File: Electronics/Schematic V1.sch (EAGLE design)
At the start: 2 parts, among them J1 SSW-130-01-G-S, J2 SSW-130-01-G-S

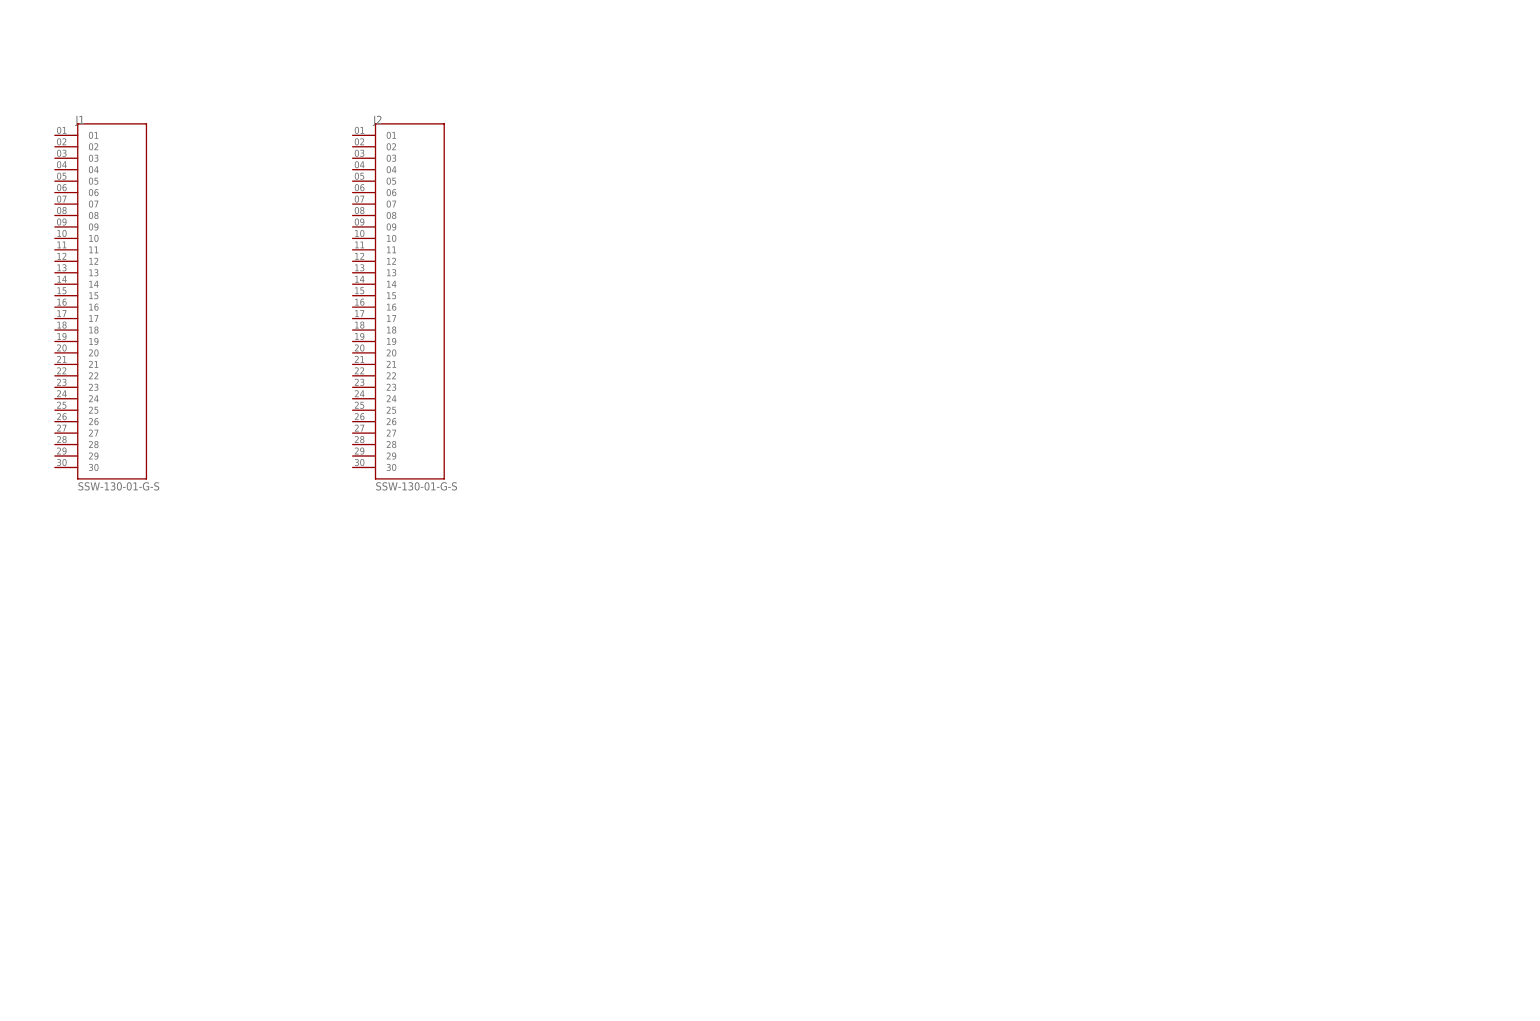
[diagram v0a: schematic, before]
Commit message: Added BOM File & Updated Schematic
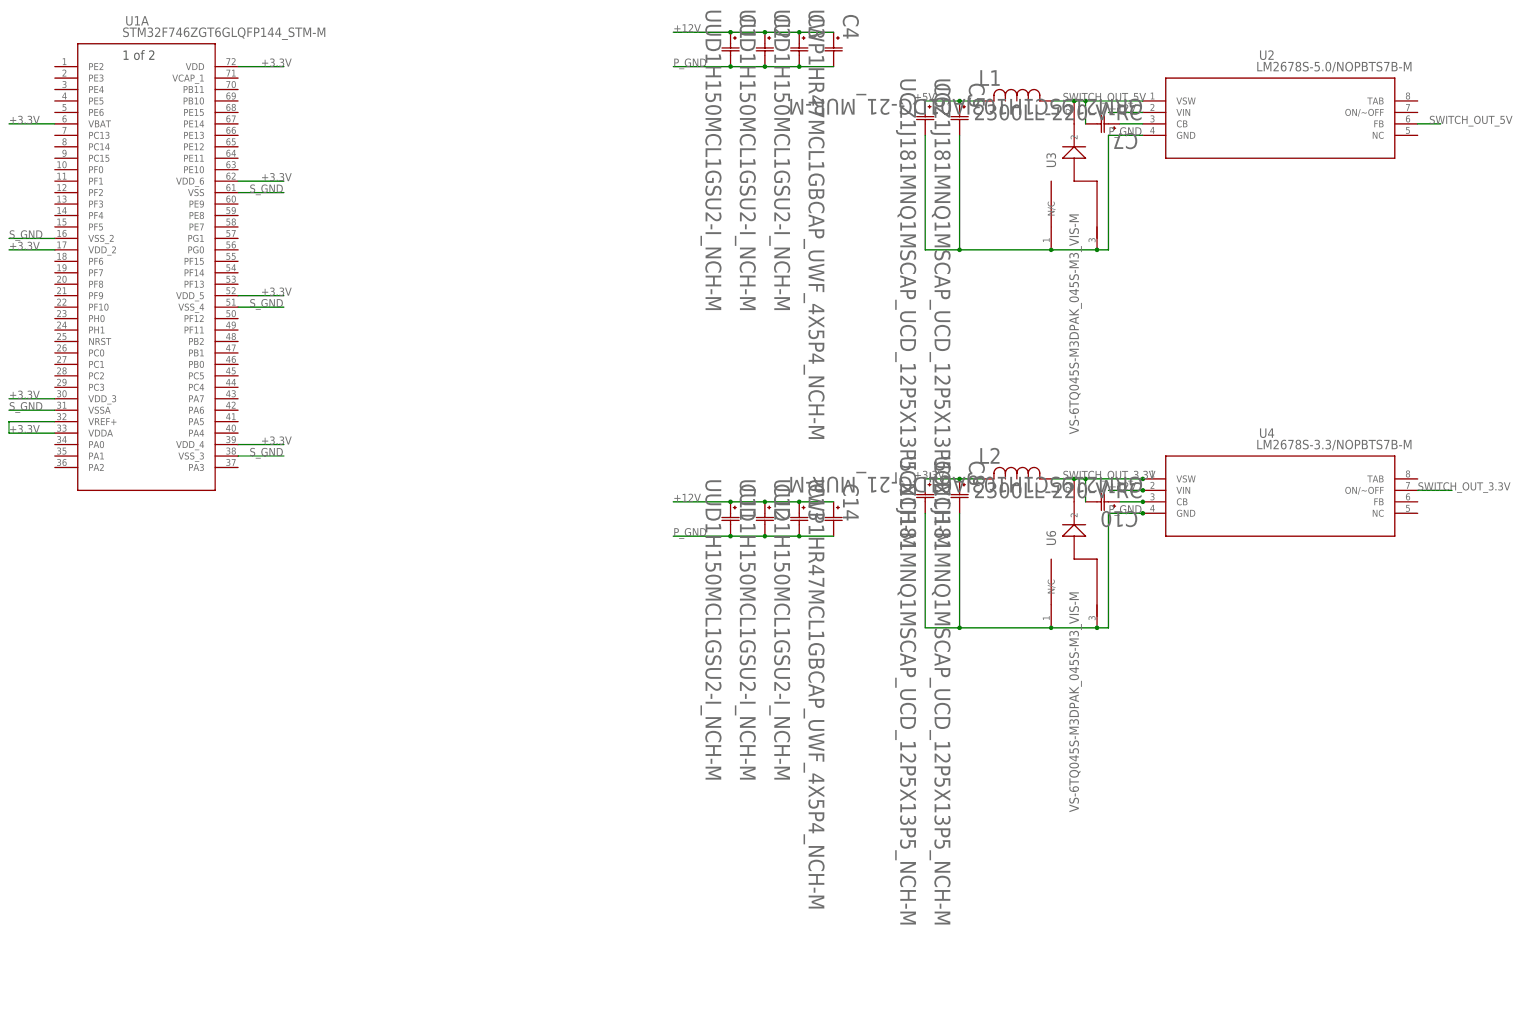
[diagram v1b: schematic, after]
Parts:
- removed J1, J2: SSW-130-01-G-S, SSW-130-01-G-S:SSW-130-01-G-S
- added C1, C11, C12, C13, C2, C3: UUD1H150MCL1GSU2-I_NCH-M, SSW-130-01-G-S:UUD1H150MCL1GSU2-I_NCH-M
- added C10, C7: GRM2195C1H103JA01DG-21_MUR-M, SSW-130-01-G-S:GRM2195C1H103JA01DG-21_MUR-M
- added C14, C4: UWP1HR47MCL1GBCAP_UWF_4X5P4_NCH-M, SSW-130-01-G-S:UWP1HR47MCL1GBCAP_UWF_4X5P4_NCH-M
- added C5, C6, C8, C9: UCZ1J181MNQ1MSCAP_UCD_12P5X13P5_NCH-M, SSW-130-01-G-S:UCZ1J181MNQ1MSCAP_UCD_12P5X13P5_NCH-M
- added L1, L2: 2300LL-220-V-RC, SSW-130-01-G-S:2300LL-220-V-RC
- added U1: STM32F746ZGT6GLQFP144_STM-M, SSW-130-01-G-S:STM32F746ZGT6GLQFP144_STM-M
- added U2: LM2678S-5.0/NOPBTS7B-M, SSW-130-01-G-S:LM2678S-5.0/NOPBTS7B-M
- added U3, U6: VS-6TQ045S-M3DPAK_045S-M3_VIS-M, SSW-130-01-G-S:VS-6TQ045S-M3DPAK_045S-M3_VIS-M
- added U4: LM2678S-3.3/NOPBTS7B-M, SSW-130-01-G-S:LM2678S-3.3/NOPBTS7B-M
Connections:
- new net +12V: C1.1, C11.1, C12.1, C13.1, C14.1, C2.1, C3.1, C4.1, U2.VIN, U4.VIN
- new net +3.3V: C8.1, C9.1, L2.2, U1A.VBAT, U1A.VDD, U1A.VDDA, U1A.VDD_2, U1A.VDD_3, U1A.VDD_4, U1A.VDD_5, U1A.VDD_6, U1A.VREF+
- new net +5V: C5.1, C6.1, L1.2
- new net N$1: C10.1, U4.CB
- new net N$2: C7.1, U2.CB
- new net P_GND: C1.2, C11.2, C12.2, C13.2, C14.2, C2.2, C3.2, C4.2, C5.2, C6.2, C8.2, C9.2, U2.GND, U3.ANODE, U3.N/C, U4.GND, U6.ANODE, U6.N/C
- new net SWITCH_OUT_3.3V: C10.2, L2.1, U4.ON/~OFF, U4.VSW, U6.2
- new net SWITCH_OUT_5V: C7.2, L1.1, U2.FB, U2.VSW, U3.2
- new net S_GND: U1A.VSS, U1A.VSSA, U1A.VSS_2, U1A.VSS_3, U1A.VSS_4

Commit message: Added A4 + Updated Schematic
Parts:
- added C15, C16, C17, C18, C19, C20, C21, C22, C23, C24, C25, C26, C27, C28, C29, C30, C32: 0.1uF, SparkFun-Capacitors:1.0UF-0805-25V-10%
- added C31, C33: 1.0uF, SparkFun-Capacitors:1.0UF-0805-25V-10%
- added C34, C35: 2.2uF, SparkFun-Capacitors:2.2UF-0805-25V-(+80/-20%)
- added C36: 4.7uF, SparkFun-Capacitors:2.2UF-0805-25V-(+80/-20%)
- added R1: 33k, SparkFun-Resistors:33KOHM-0603-1/10W-1%
- added R2: 68.1k, SparkFun-Resistors:68.1KOHM-0603-1/10W-1%
- added U5: STM32F207VGT6TR, SSW-130-01-G-S:STM32F207VGT6TR
- U1: value STM32F746ZGT6GLQFP144_STM-M -> STM32F207VGT6TR; device SSW-130-01-G-S:STM32F746ZGT6GLQFP144_STM-M -> SSW-130-01-G-S:STM32F207VGT6TR
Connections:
- new net N$4: C35.2, U5C.VCAP_1
- new net N$5: C34.2, U5C.VCAP_2
- new net S_GND1: C32.1, C33.1
- new net V_ON: R1.2, R2.1, U2.ON/~OFF, U4.ON/~OFF
- net +12V: now also R2.2
- net +3.3V: now also C15.2, C16.2, C17.2, C18.2, C19.2, C20.2, C21.2, C22.2, C23.2, C24.2, C25.2, C26.2, C27.2, C28.2, C29.2, C30.2, C31.2, C32.2, C33.2, C36.2, U5C.VBAT, U5C.VDD, U5C.VDDA, U5C.VDD_2, U5C.VDD_3, U5C.VDD_4, U5C.VDD_5, U5C.VDD_6, U5C.VREF+; no longer U1A.VBAT, U1A.VDD, U1A.VDDA, U1A.VDD_2, U1A.VDD_3, U1A.VDD_4, U1A.VDD_5, U1A.VDD_6, U1A.VREF+
- net P_GND: now also R1.1
- net SWITCH_OUT_3.3V: now also U4.FB; no longer U4.ON/~OFF
- net S_GND: now also C15.1, C16.1, C17.1, C18.1, C19.1, C20.1, C21.1, C22.1, C23.1, C24.1, C25.1, C26.1, C27.1, C28.1, C29.1, C30.1, C31.1, C34.1, C35.1, C36.1, U5C.VSS, U5C.VSSA, U5C.VSS_2, U5C.VSS_3; no longer U1A.VSS, U1A.VSSA, U1A.VSS_2, U1A.VSS_3, U1A.VSS_4
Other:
- note added: "STM32 Power Pins"
- note added: "VDD Capacitors"

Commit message: Updated Schematic with Main Features
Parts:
- added C37: 10uF, SparkFun-Capacitors:10UF-0805-10V-10%
- added C38: 0.1uF, rcl:C-USC0805
- added C39: 4.7nF, rcl:C-USC0805
- added C40: 10pF, SparkFun-Capacitors:10UF-0805-10V-10%
- added C41, C42, C43, C44: 4.7uF, rcl:C-USC0805
- added C45: (no value), rcl:C-USC0805
- added C46, C47, C48, C49, C54, C59: 1.0uF, SparkFun-Capacitors:1.0UF-0805-25V-10%
- added C50, C51, C52, C53, C55, C56, C57, C58: 0.1uF, SparkFun-Capacitors:1.0UF-0805-25V-10%
- added CR1: SL03-GS18CR_SL03_VIS-M, SSW-130-01-G-S:SL03-GS18CR_SL03_VIS-M
- added D1, D2, D3, D4, D5, D6: 250mA/100V, SparkFun-DiscreteSemi:DIODE-BAS16J
- added J1: PJ-202AH, SSW-130-01-G-S:PJ-202AH
- added L3: 7443551131IND_1365-WE-HCI_WRE-M, SSW-130-01-G-S:7443551131IND_1365-WE-HCI_WRE-M
- added R10, R12, R20, R22: 37k, rcl:R-US_R0805
- added R11, R13, R16, R19, R21, R23, R26, R9: 10k, rcl:R-US_R0805
- added R14, R15, R24, R25: 73k, rcl:R-US_R0805
- added R17, R18, R27, R28, R29, R30: 2.25k, rcl:R-US_R0805
- added R3: 10, rcl:R-US_R0805
- added R31, R32, R33, R34, R35, R36, R37, R38: 330, rcl:R-US_R0805
- added R39, R42, R45, R48, R51, R54, R57, R60: 500, rcl:R-US_R0805
- added R4: 1.5M, rcl:R-US_R0805
- added R40, R43, R46, R49, R52, R55, R58, R61: 75k, rcl:R-US_R0805
- added R41, R44, R47, R50, R53, R56, R59, R62: 25k, rcl:R-US_R0805
- added R5: 121k, rcl:R-US_R0805
- added R6: 100k, rcl:R-US_R0805
- added R7: 3352T-1-105LF, SSW-130-01-G-S:3352T-1-105LF
- added R8: 89k, rcl:R-US_R0805
- added U10, U17, U18, U19: SN65LBC175ADD16-M, SSW-130-01-G-S:SN65LBC175ADD16-M
- added U11, U8: OPA4205APWRTSSOP14_PW_R-PDSO-G14_TEX-M, SSW-130-01-G-S:OPA4205APWRTSSOP14_PW_R-PDSO-G14_TEX-M
- added U12, U7: SN75ALS174ADWRDW20-M, SSW-130-01-G-S:SN75ALS174ADWRDW20-M
- added U13, U14: SN75468DRD0016A_M, SSW-130-01-G-S:SN75468DRD0016A_M
- added U15, U16: ACSL-6400-00TESOIC_6400-00TE-M, SSW-130-01-G-S:ACSL-6400-00TESOIC_6400-00TE-M
- added U9: TPS63700DRCR, SSW-130-01-G-S:TPS63700DRCR
- L1, L2: value 2300LL-220-V-RC -> 2300HT-220-H-RC; device SSW-130-01-G-S:2300LL-220-V-RC -> SSW-130-01-G-S:2300HT-220-H-RC
- R1: value 33k -> 25k
- R2: value 68.1k -> 75k; device SparkFun-Resistors:68.1KOHM-0603-1/10W-1% -> rcl:R-US_R0805
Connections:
- removed net +12V: C1.1, C11.1, C12.1, C13.1, C14.1, C2.1, C3.1, C4.1, R2.2, U2.VIN, U4.VIN
- removed net S_GND1: C32.1, C33.1
- new net +14V: C1.1, C11.1, C12.1, C13.1, C14.1, C2.1, C3.1, C4.1, J1.1, R2.2, R39.2, R40.2, R42.2, R43.2, R45.2, R46.2, R48.2, R49.2, R51.2, R52.2, R54.2, R55.2, R57.2, R58.2, R60.2, R61.2, R8.2, U2.VIN, U4.VIN, U8.V+
- new net +24V: R17.2, R18.2, R27.2, R28.2, R29.2, R30.2, U13.COM, U14.COM
- new net -15V: C41.1, C42.1, C43.1, C44.1, CR1.2, R4.1, R6.2, U8.V-, U9.OUT
- new net 1.65V_REF: R13.1, R19.1, R23.1, R9.1, U8.-IN_1, U8.OUT_1
- new net 14V-24V_GND: J1.2, J1.3, R1.1, U13.E, U14.E
- new net ABS_ENC_OUT_GPIO_1: U10.4Y
- new net ABS_ENC_OUT_GPIO_2: U17.4Y
- new net ABS_ENC_OUT_HI_1: R33.1, U10.4A
- new net ABS_ENC_OUT_HI_2: R37.1, U17.4A
- new net ABS_ENC_OUT_LO_1: R33.2, U10.4B
- new net ABS_ENC_OUT_LO_2: R37.2, U17.4B
- new net ALARM_RST_AN_1: U13.5C
- new net ALARM_RST_AN_2: U14.5C
- new net ALARM_RST_GPIO_1: U13.5B
- new net ALARM_RST_GPIO_2: U14.5B
- new net ALO_AN_A_1: D1.A, U15.CATHODE1
- new net ALO_AN_A_2: D4.A, U16.CATHODE1
- new net ALO_AN_B_1: D2.A, U15.CATHODE2
- new net ALO_AN_B_2: D5.A, U16.CATHODE2
- new net ALO_AN_C_1: D3.A, U15.CATHODE3
- new net ALO_AN_C_2: D6.A, U16.CATHODE3
- new net ALO_GPIO_A_1: U15.V01
- new net ALO_GPIO_A_2: U16.V01
- new net ALO_GPIO_B_1: U15.V02
- new net ALO_GPIO_B_2: U16.V02
- new net ALO_GPIO_C_1: U15.V03
- new net ALO_GPIO_C_2: U16.V03
- new net CLR_EN_GPIO: U12.3/42N, U7.3/42N
- new net CLR_GPIO_1: U7.3A
- new net CLR_GPIO_2: U12.3A
- new net CLR_HI_1: U7.3Y
- new net CLR_HI_2: U12.3Y
- new net CLR_LO_1: U7.3Z
- new net CLR_LO_2: U12.3Z
- new net DIR_GPIO_1: U7.2A
- new net DIR_GPIO_2: U12.2A
- new net DIR_HI_1: U7.2Y
- new net DIR_HI_2: U12.2Y
- new net DIR_LO_1: U7.2Z
- new net DIR_LO_2: U12.2Z
- new net ENC_PUL_OUT_A_GPIO_1: U10.1Y
- new net ENC_PUL_OUT_A_GPIO_2: U17.1Y
- new net ENC_PUL_OUT_A_HI_1: R31.1, U10.1A
- new net ENC_PUL_OUT_A_HI_2: R35.1, U17.1A
- new net ENC_PUL_OUT_A_LO_1: R31.2, U10.1B
- new net ENC_PUL_OUT_A_LO_2: R35.2, U17.1B
- new net ENC_PUL_OUT_B_GPIO_1: U10.2Y
- new net ENC_PUL_OUT_B_GPIO_2: U17.2Y
- new net ENC_PUL_OUT_B_HI_1: R32.2, U10.2A
- new net ENC_PUL_OUT_B_HI_2: R36.2, U17.2A
- new net ENC_PUL_OUT_B_LO_1: R32.1, U10.2B
- new net ENC_PUL_OUT_B_LO_2: R36.1, U17.2B
- new net ENC_PUL_OUT_C_GPIO_1: U10.3Y
- new net ENC_PUL_OUT_C_GPIO_2: U17.3Y
- new net ENC_PUL_OUT_C_HI_1: R34.2, U10.3A
- new net ENC_PUL_OUT_C_HI_2: R38.2, U17.3A
- new net ENC_PUL_OUT_C_LO_1: R34.1, U10.3B
- new net ENC_PUL_OUT_C_LO_2: R38.1, U17.3B
- new net FRWD_DRIVE_EN_AN_1: U13.3C
- new net FRWD_DRIVE_EN_AN_2: U14.3C
- new net FRWD_DRIVE_EN_GPIO_1: U13.3B
- new net FRWD_DRIVE_EN_GPIO_2: U14.3B
- new net FRWD_EX_TORQUE_LIM_EN_AN_1: U13.6C
- new net FRWD_EX_TORQUE_LIM_EN_AN_2: U14.6C
- new net FRWD_EX_TORQUE_LIM_EN_GPIO_1: U13.6B
- new net FRWD_EX_TORQUE_LIM_EN_GPIO_2: U14.6B
- new net GEN_PURPOSE_OUT_GPIO_A_1: U18.1Y
- new net GEN_PURPOSE_OUT_GPIO_A_2: U19.1Y
- new net GEN_PURPOSE_OUT_GPIO_B_1: U18.2Y
- new net GEN_PURPOSE_OUT_GPIO_B_2: U19.2Y
- new net GEN_PURPOSE_OUT_GPIO_C_1: U18.3Y
- new net GEN_PURPOSE_OUT_GPIO_C_2: U19.3Y
- new net GEN_PURPOSE_OUT_HI_A_1: R39.1, U18.1A
- new net GEN_PURPOSE_OUT_HI_A_2: R51.1, U19.1A
- new net GEN_PURPOSE_OUT_HI_B_1: R42.1, U18.2A
- new net GEN_PURPOSE_OUT_HI_B_2: R54.1, U19.2A
- new net GEN_PURPOSE_OUT_HI_C_1: R45.1, U18.3A
- new net GEN_PURPOSE_OUT_HI_C_2: R57.1, U19.3A
- new net GEN_PURPOSE_OUT_LO_A_1: C50.2, R40.1, R41.2, U18.1B
- new net GEN_PURPOSE_OUT_LO_A_2: C55.2, R52.1, R53.2, U19.1B
- new net GEN_PURPOSE_OUT_LO_B_1: C51.2, R43.1, R44.2, U18.2B
- new net GEN_PURPOSE_OUT_LO_B_2: C56.2, R55.1, R56.2, U19.2B
- new net GEN_PURPOSE_OUT_LO_C_1: C52.2, R46.1, R47.2, U18.3B
- new net GEN_PURPOSE_OUT_LO_C_2: C57.2, R58.1, R59.2, U19.3B
- new net N$10: C40.2, R4.2, R5.1, U9.FB
- new net N$11: C40.1, R6.1
- new net N$12: R7.2, U8.+IN_1
- new net N$13: R7.3, R8.1
- new net N$15: R11.2, R12.2, U8.+IN_2
- new net N$17: R13.2, R14.2, U8.-IN_4
- new net N$18: R15.2, R16.2, U8.+IN_4
- new net N$20: D1.C, R17.1, U15.ANODE1
- new net N$21: R19.2, R20.2, U11.-IN_2
- new net N$22: R21.2, R22.2, U11.+IN_2
- new net N$23: R23.2, R24.2, U11.-IN_4
- new net N$24: R25.2, R26.2, U11.+IN_4
- new net N$25: D2.C, R18.1, U15.ANODE2
- new net N$26: D3.C, R27.1, U15.ANODE3
- new net N$27: D4.C, R28.1, U16.ANODE1
- new net N$28: D5.C, R29.1, U16.ANODE2
- new net N$29: D6.C, R30.1, U16.ANODE3
- new net N$3: C39.1, U9.COMP
- new net N$6: C38.1, R3.1, U9.EN, U9.VIN
- new net N$7: CR1.1, L3.2, U9.SW
- new net N$8: R10.2, R9.2, U8.-IN_2
- new net N$9: C45.1, R5.2, U9.VREF
- new net POS_EN_GPIO: U12.1/2EN, U7.1/2EN
- new net PROP_CONTROL_EN_AN_1: U13.2C
- new net PROP_CONTROL_EN_AN_2: U14.2C
- new net PROP_CONTROL_EN_GPIO_1: U13.2B
- new net PROP_CONTROL_EN_GPIO_2: U14.2B
- new net PULSE_GPIO_1: U7.1A
- new net PULSE_GPIO_2: U12.1A
- new net PULSE_HI_1: U7.1Y
- new net PULSE_HI_2: U12.1Y
- new net PULSE_LO_1: U7.1Z
- new net PULSE_LO_2: U12.1Z
- new net REVERSE_DRIVE_EN_AN_1: U13.4C
- new net REVERSE_DRIVE_EN_AN_2: U14.4C
- new net REVERSE_DRIVE_EN_GPIO_1: U13.4B
- new net REVERSE_DRIVE_EN_GPIO_2: U14.4B
- new net REVERSE_EX_TORQUE_LIM_EN_AN_1: U13.7C
- new net REVERSE_EX_TORQUE_LIM_EN_AN_2: U14.7C
- new net REVERSE_EX_TORQUE_LIM_EN_GPIO_1: U13.7B
- new net REVERSE_EX_TORQUE_LIM_EN_GPIO_2: U14.7B
- new net SERVO_ALARM_OUT_GPIO_1: U18.4Y
- new net SERVO_ALARM_OUT_GPIO_2: U19.4Y
- new net SERVO_ALARM_OUT_HI_1: R48.1, U18.4A
- new net SERVO_ALARM_OUT_HI_2: R60.1, U19.4A
- new net SERVO_ALARM_OUT_LO_1: C53.2, R49.1, R50.2, U18.4B
- new net SERVO_ALARM_OUT_LO_2: C58.2, R61.1, R62.2, U19.4B
- new net SERVO_EN_AN_1: U13.1C
- new net SERVO_EN_AN_2: U14.1C
- new net SERVO_EN_GPIO_1: U13.1B
- new net SERVO_EN_GPIO_2: U14.1B
- new net SPEED_ANALOG_1: R12.1, U8.OUT_2
- new net SPEED_ANALOG_2: R22.1, U11.OUT_2
- new net SPEED_DAC_1: R11.1
- new net SPEED_DAC_2: R21.1
- new net TORQUE_ANALOG_1: R15.1, U8.OUT_4
- new net TORQUE_ANALOG_2: R25.1, U11.OUT_4
- new net TORQUE_DAC_1: R16.1
- new net TORQUE_DAC_2: R26.1
- net +5V: now also C37.2, C46.2, C47.2, C48.2, C49.2, C54.2, C59.2, R3.2, U10.VCC, U12.VCC, U15.VDD, U15.VDD_2, U16.VDD, U16.VDD_2, U17.VCC, U18.VCC, U19.VCC, U7.VCC, U9.IN
- net P_GND: now also C37.1, C38.2, C39.2, C41.2, C42.2, C43.2, C44.2, C45.2, L3.1, R10.1, R14.1, R20.1, R24.1, R7.1, U9.GND, U9.PS_GND; no longer R1.1
- net S_GND: now also C32.1, C33.1, C46.1, C47.1, C48.1, C49.1, C50.1, C51.1, C52.1, C53.1, C54.1, C55.1, C56.1, C57.1, C58.1, C59.1, R41.1, R44.1, R47.1, R50.1, R53.1, R56.1, R59.1, R62.1, U10.GND, U12.GND, U15.GND, U15.GND_2, U16.GND, U16.GND_2, U17.GND, U18.GND, U19.GND, U7.GND
- net V_ON: now also U10.1/2EN, U10.3/4EN, U17.1/2EN, U17.3/4EN, U18.1/2EN, U18.3/4EN, U19.1/2EN, U19.3/4EN
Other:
- note added: "-15V Boost Inverter Controller Circuit"
- note added: "14V Input"
- note added: "3.3V Buck Controller Circuit"
- note added: "5V Buck Controller Circuit"
- note added: "DAC <-> Speed + Torque Control"
- note added: "Enable Buck Controller, Encoder, Gen Out"
- note added: "INPUTS TO SERVO"
- note added: "Line Driver IC (Position Control)"
- note added: "Line Receiver IC (Encoder Pulses)"
- note added: "Line Receiver IC (General Purpose Output)"
- note added: "NPN Transistor Array (General-Purpose Sequency Inputs)"
- note added: "OUTPUTS FROM SERVO"
- note added: "Photocoupler IC (Alarm Code Signals)"
- note added: "STM32 IO Pins"

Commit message: Updated Schematic
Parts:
- added C60, C61: 0.1uF, SparkFun-Capacitors:1.0UF-0805-25V-10%
- added J2: PJ-025, SSW-130-01-G-S:PJ-025
- added R63, R64, R65, R66, R67, R68: 1k, rcl:R-US_R0805
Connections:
- net +14V: now also J2.1; no longer J1.1
- net +24V: now also J1.1
- net +3.3V: now also C60.2, C61.2, R63.2, R64.2, R65.2, R66.2, R67.2, R68.2, U15.VDD, U15.VDD_2, U16.VDD, U16.VDD_2
- net +5V: no longer U15.VDD, U15.VDD_2, U16.VDD, U16.VDD_2
- net 14V-24V_GND: now also J2.2, J2.3
- net ALO_GPIO_A_1: now also R66.1
- net ALO_GPIO_A_2: now also R63.1
- net ALO_GPIO_B_1: now also R67.1
- net ALO_GPIO_B_2: now also R64.1
- net ALO_GPIO_C_1: now also R68.1
- net ALO_GPIO_C_2: now also R65.1
- net S_GND: now also C60.1, C61.1
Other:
- moved on the sheet: D4, D5, D6, R28, R29, R30, U16
